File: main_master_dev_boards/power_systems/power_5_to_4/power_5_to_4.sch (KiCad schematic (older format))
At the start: 18 parts

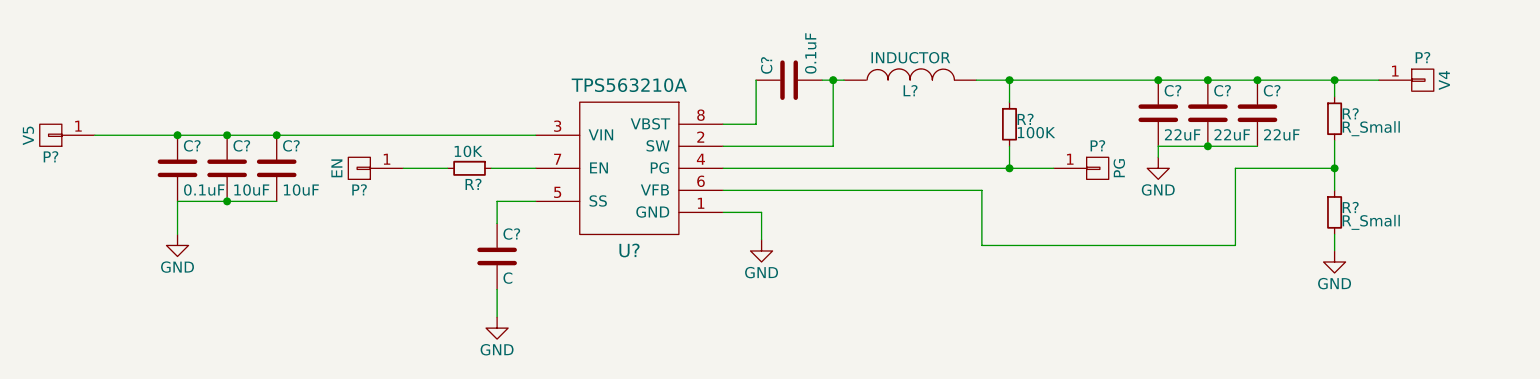
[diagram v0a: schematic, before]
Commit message: Started working on 4 to 5 boost dev board
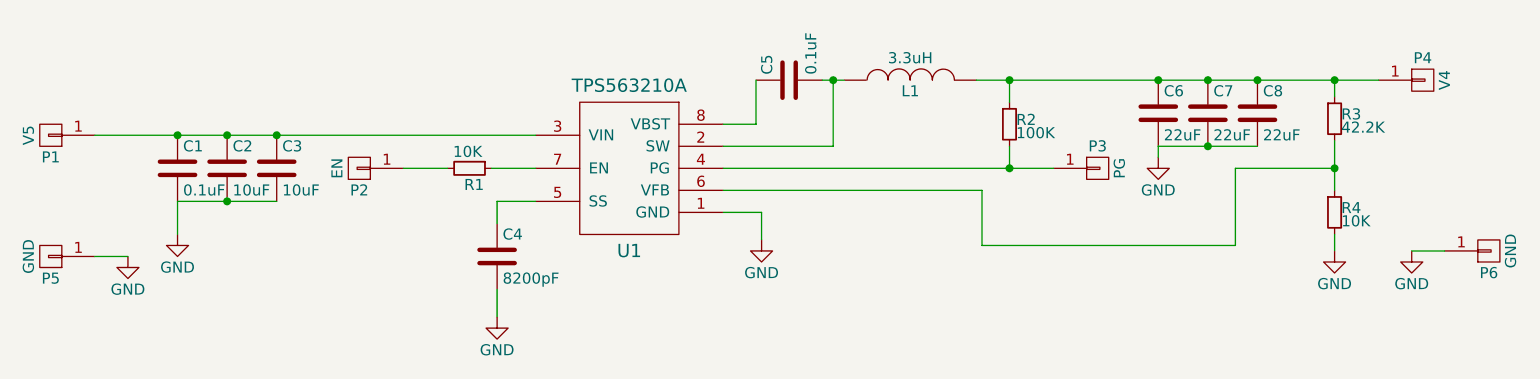
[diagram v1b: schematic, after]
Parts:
- added P5, P6: GND, pinheaders:pinhead-01x01_3x1_square, symbol CONN_01X01
- C1, C2, C3, C5, C6, C7, C8: renamed from C?; footprint (none) -> Capacitors_SMD:C_0805_HandSoldering
- C4: renamed from C?; value C -> 8200pF; footprint (none) -> Capacitors_SMD:C_0805_HandSoldering
- L1: renamed from L?; value INDUCTOR -> 3.3uH; footprint (none) -> Bourns:SRP4020TA
- P1, P2, P3, P4: renamed from P?; footprint (none) -> pinheaders:pinhead-01x01_3x1
- R1, R2: renamed from R?; footprint (none) -> Resistors_SMD:R_0805_HandSoldering
- R3: renamed from R?; value R_Small -> 42.2K; footprint (none) -> Resistors_SMD:R_0805_HandSoldering
- R4: renamed from R?; value R_Small -> 10K; footprint (none) -> Resistors_SMD:R_0805_HandSoldering
- U1: renamed from U?; footprint (none) -> TO_SOT_Packages_SMD:SOT-23-8_Handsoldering
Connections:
- net GND: now also P5.1 (P1), P6.1 (P1)
